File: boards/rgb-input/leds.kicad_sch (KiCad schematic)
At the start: 1 part, among them J46 RGB

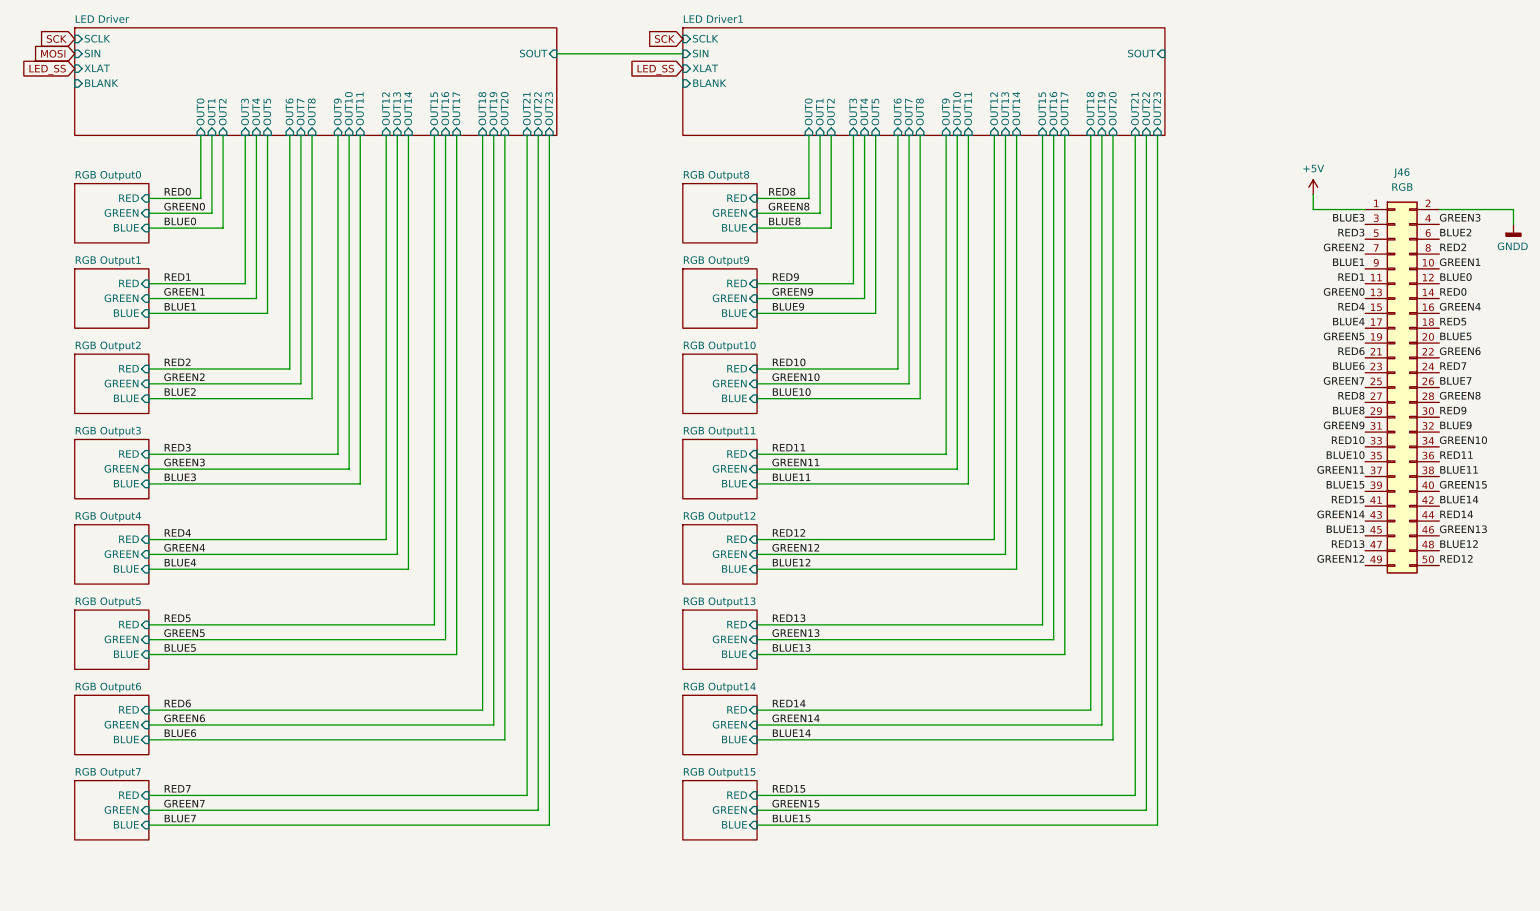
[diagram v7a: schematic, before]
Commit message: first pass on redesign of the rgb input board
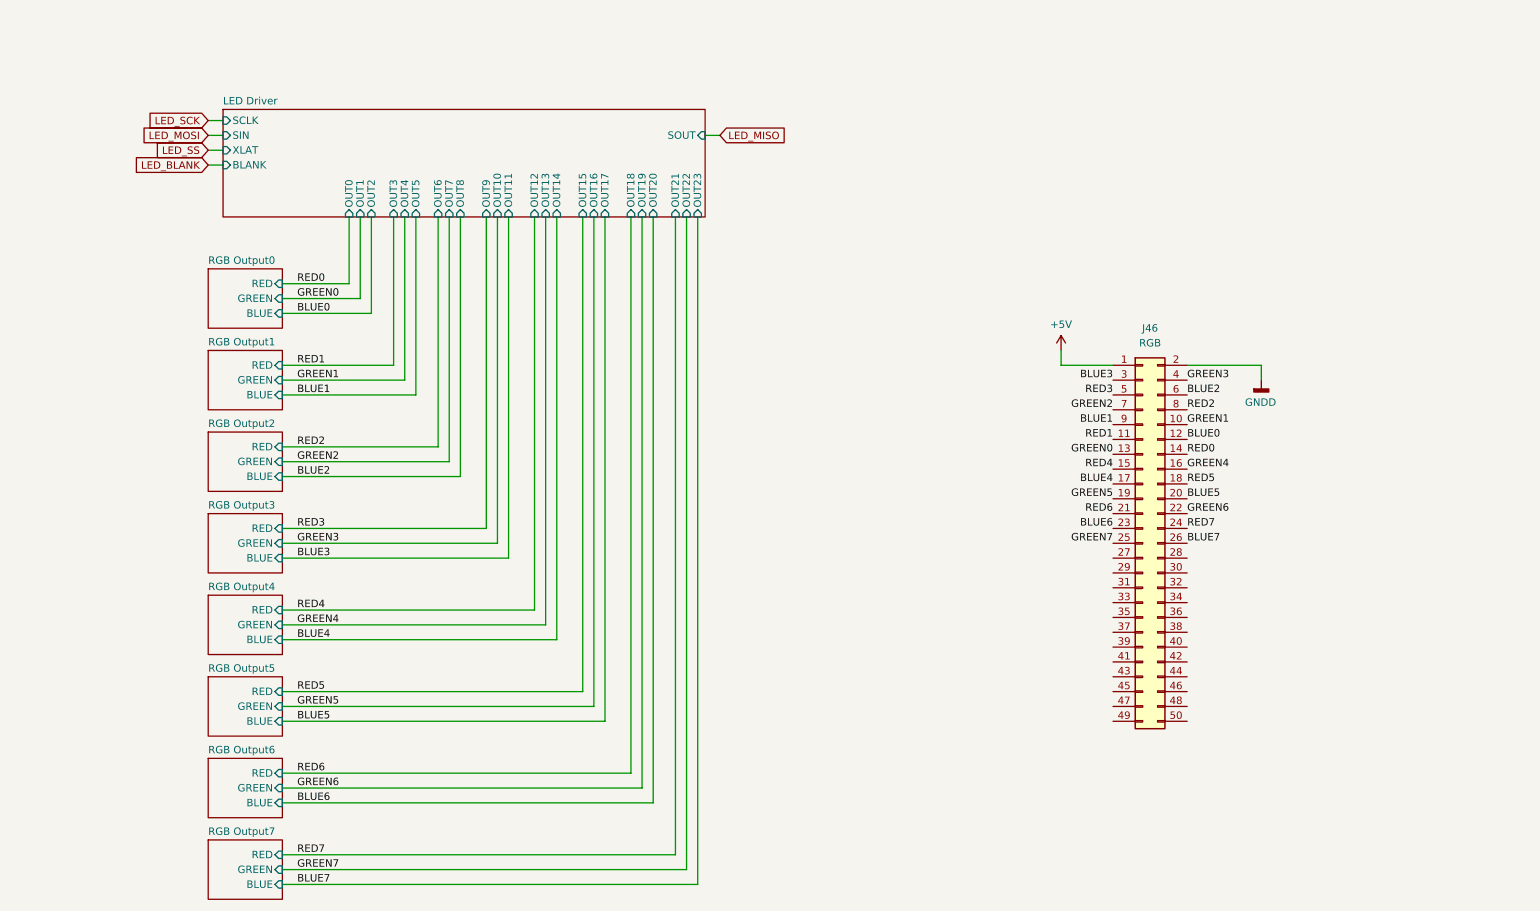
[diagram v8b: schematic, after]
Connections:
- net BLUE10: no longer names the net of J46.35 (Pin_35)
- net BLUE11: no longer names the net of J46.38 (Pin_38)
- net BLUE12: no longer names the net of J46.48 (Pin_48)
- net BLUE13: no longer names the net of J46.45 (Pin_45)
- net BLUE14: no longer names the net of J46.42 (Pin_42)
- net BLUE15: no longer names the net of J46.39 (Pin_39)
- net BLUE8: no longer names the net of J46.29 (Pin_29)
- net BLUE9: no longer names the net of J46.32 (Pin_32)
- net GREEN10: no longer names the net of J46.34 (Pin_34)
- net GREEN11: no longer names the net of J46.37 (Pin_37)
- net GREEN12: no longer names the net of J46.49 (Pin_49)
- net GREEN13: no longer names the net of J46.46 (Pin_46)
- net GREEN14: no longer names the net of J46.43 (Pin_43)
- net GREEN15: no longer names the net of J46.40 (Pin_40)
- net GREEN8: no longer names the net of J46.28 (Pin_28)
- net GREEN9: no longer names the net of J46.31 (Pin_31)
- net RED10: no longer names the net of J46.33 (Pin_33)
- net RED11: no longer names the net of J46.36 (Pin_36)
- net RED12: no longer names the net of J46.50 (Pin_50)
- net RED13: no longer names the net of J46.47 (Pin_47)
- net RED14: no longer names the net of J46.44 (Pin_44)
- net RED15: no longer names the net of J46.41 (Pin_41)
- net RED8: no longer names the net of J46.27 (Pin_27)
- net RED9: no longer names the net of J46.30 (Pin_30)
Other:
- removed sheet LED Driver1
- removed sheet RGB Output10
- removed sheet RGB Output11
- removed sheet RGB Output12
- removed sheet RGB Output13
- removed sheet RGB Output14
- removed sheet RGB Output15
- removed sheet RGB Output8
- removed sheet RGB Output9
- moved on the sheet: J46
